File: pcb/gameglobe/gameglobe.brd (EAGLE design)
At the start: 49.5 x 99.1 mm, 12 parts

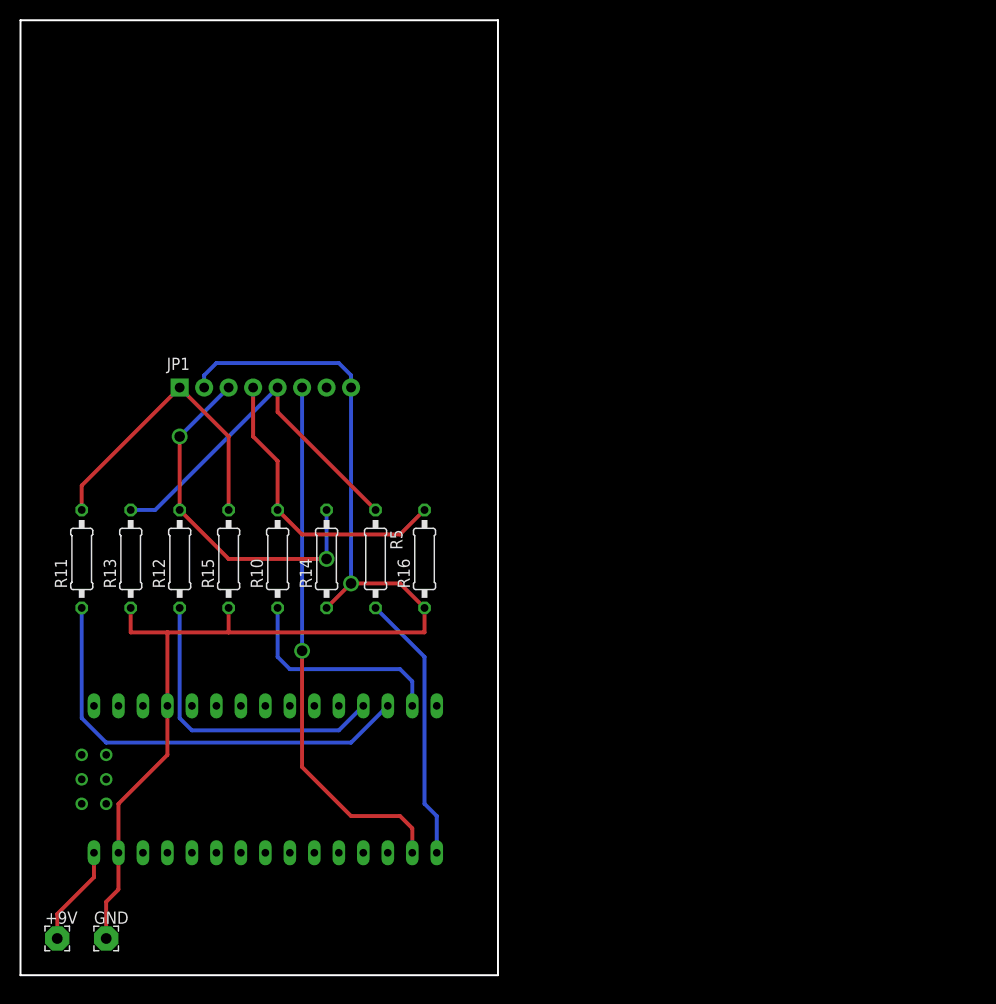
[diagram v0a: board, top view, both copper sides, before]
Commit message: BOM is sortof complete, and PCB is more complete-ish now
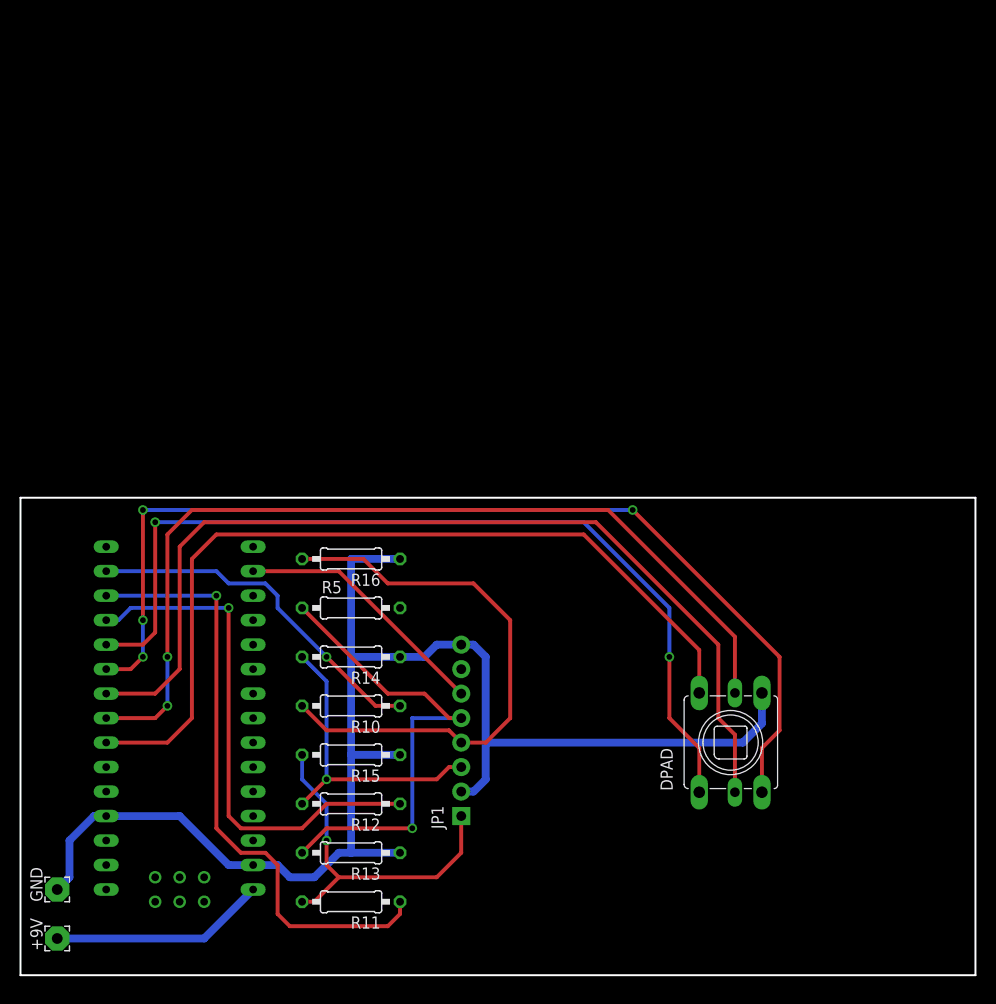
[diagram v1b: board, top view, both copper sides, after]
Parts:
- added DPAD: SKQUCAA010, gamaral:SKQU
- moved JP1 53.2 mm to (45.7, 16.5), turned to 90 degrees
- moved R11 45.2 mm to (34.3, 7.62), turned to 180 degrees
- moved R13 38.1 mm to (34.3, 12.7), turned to 180 degrees
- moved R12 31.0 mm to (34.3, 17.8), turned to 180 degrees
- moved R15 24.0 mm to (34.3, 22.9), turned to 180 degrees
- moved R10 17.0 mm to (34.3, 27.9), turned to 180 degrees
- moved R14 10.5 mm to (34.3, 33.0), turned to 180 degrees
- moved R16 7.62 mm to (34.3, 43.2), turned to 180 degrees
- moved GND 7.18 mm to (3.81, 8.89), turned to 90 degrees
- moved U$1 5.68 mm to (14.0, 17.8), turned to 0 degrees
- moved R5 5.68 mm to (34.3, 38.1), turned to 0 degrees
- turned +9V to 90 degrees
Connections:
- new net N$10: DPAD.CENTER, U$1.D4
- new net N$5: DPAD.UP, U$1.D8
- new net N$6: DPAD.DOWN, U$1.D7
- new net N$8: DPAD.LEFT, U$1.D6
- new net N$9: DPAD.RIGHT, U$1.D5
- net GND: now also DPAD.COMMON
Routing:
- net N$6: track 0.00 -> 106.7 mm, vias 0 -> 4
- net N$8: track 0.00 -> 99.6 mm
- net N$9: track 0.00 -> 95.9 mm, vias 0 -> 2
- net N$5: track 0.00 -> 94.5 mm, vias 0 -> 2
- net N$10: track 0.00 -> 89.6 mm
- net VCC_LCD: track 56.0 -> 26.9 mm, vias 1 -> 0
- net N$1: track 28.0 -> 0.00 mm
- net DIN_LCD: track 31.1 -> 58.6 mm
- net GND: track 123.9 -> 148.7 mm, vias 1 -> 0
- net N$4: track 32.1 -> 54.2 mm, vias 0 -> 1
- net N$3: track 45.8 -> 63.6 mm, vias 0 -> 1
- net N$2: track 22.6 -> 37.0 mm, vias 0 -> 1
- net CLK_LCD: track 37.4 -> 50.2 mm, vias 0 -> 1
- net N$7: track 10.5 -> 22.4 mm
- net DC_LCD: track 37.2 -> 31.8 mm, vias 2 -> 1
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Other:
- board size 49.5 x 99.1 mm -> 99.1 x 49.5 mm

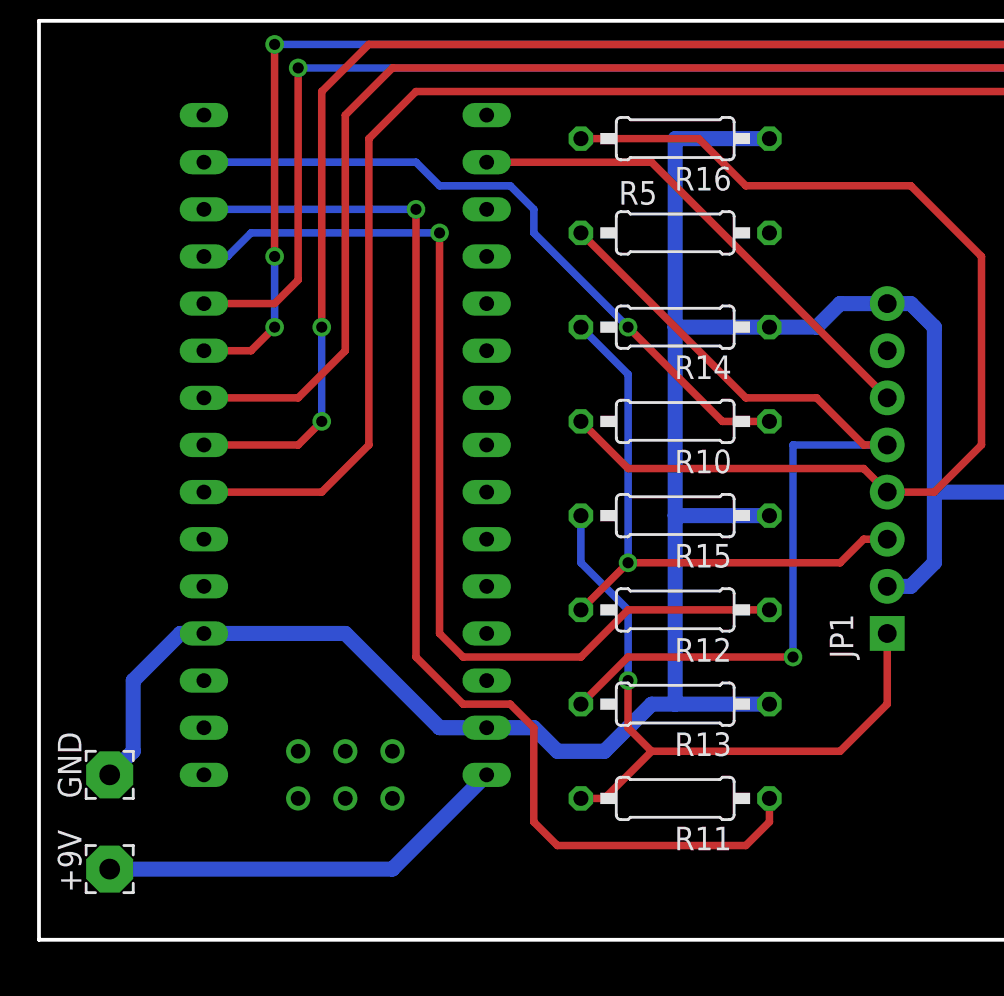
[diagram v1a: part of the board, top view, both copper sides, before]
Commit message: Add backlight wire and resistor
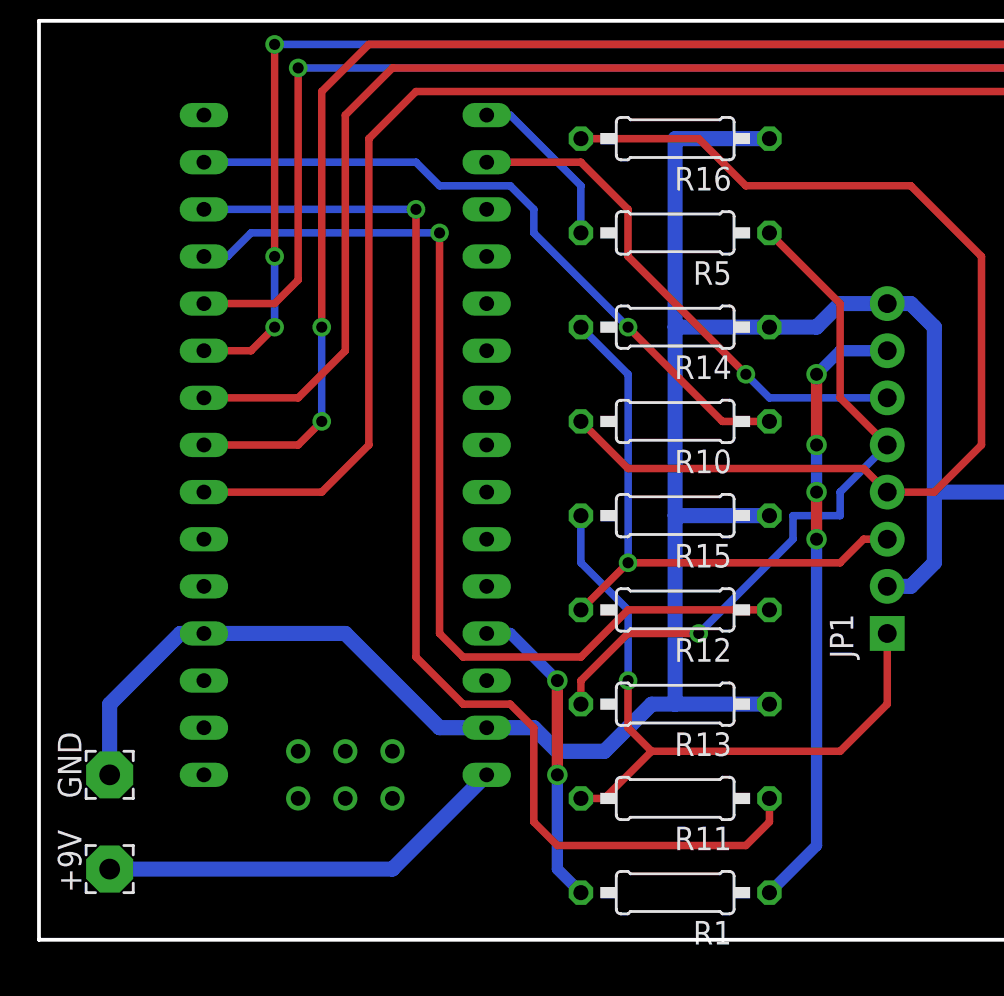
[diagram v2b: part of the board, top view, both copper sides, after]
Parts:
- added R1: 220, resistor:0207/10
- turned R5 to 180 degrees
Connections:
- removed net BL_LCD: JP1.7
- new net LED_LCD: JP1.7, R1.1
- new net N$11: R1.2, U$1.5V
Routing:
- net LED_LCD: track 0.00 -> 33.3 mm, vias 0 -> 4
- net N$11: track 0.00 -> 16.8 mm, vias 0 -> 2
- net CLK_LCD: track 50.2 -> 38.6 mm
- net N$1: track 0.00 -> 9.20 mm
- net VCC_LCD: track 26.9 -> 28.3 mm, vias 0 -> 1
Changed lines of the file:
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@@
 <element name="+9V" library="wirepad" package="2,54/1,1" value="WIREPAD2,54/1,1" x="3.81" y="3.81" rot="R90"/>
 <element name="GND" library="wirepad" package="2,54/1,1" value="WIREPAD2,54/1,1" x="3.81" y="8.89" rot="R90"/>
-<element name="R5" library="resistor" package="0207/10" value="10k" x="34.29" y="38.1"/>
+<element name="R5" library="resistor" package="0207/10" value="10k" x="34.29" y="38.1" rot="R180"/>
 <element name="R10" library="resistor" package="0207/10" value="10k" x="34.29" y="27.94" rot="R180"/>
 <element name="R11" library="resistor" package="0207/10" value="10k" x="34.29" y="7.62" rot="R180"/>
@@
 <attribute name="OC_ADAFRUIT" value="504" x="73.66" y="24.13" size="1.778" layer="27" rot="R90" display="off"/>
 </element>
+<element name="R1" library="resistor" package="0207/10" value="220" x="34.29" y="2.54" rot="R180"/>
 </elements>
 <signals>
@@
 <contactref element="GND" pad="1"/>
 <contactref element="DPAD" pad="COMMON"/>
-<wire x1="3.81" y1="8.89" x2="5.08" y2="10.16" width="0.8128" layer="16"/>
-<wire x1="5.08" y1="10.16" x2="5.08" y2="13.97" width="0.8128" layer="16"/>
-<wire x1="5.08" y1="13.97" x2="7.62" y2="16.51" width="0.8128" layer="16"/>
+<wire x1="3.81" y1="12.7" x2="7.62" y2="16.51" width="0.8128" layer="16"/>
 <wire x1="7.62" y1="16.51" x2="8.89" y2="16.51" width="0.8128" layer="16"/>
-<wire x1="8.89" y1="16.51" x2="16.51" y2="16.51" width="0.8128" layer="16"/>
+<wire x1="16.51" y1="16.51" x2="8.89" y2="16.51" width="0.8128" layer="16"/>
 <wire x1="16.51" y1="16.51" x2="21.59" y2="11.43" width="0.8128" layer="16"/>
 <wire x1="21.59" y1="11.43" x2="24.13" y2="11.43" width="0.8128" layer="16"/>
@@
 <wire x1="76.91" y1="26.11" x2="74.93" y2="24.13" width="0.8128" layer="16"/>
 <wire x1="74.93" y1="24.13" x2="48.26" y2="24.13" width="0.8128" layer="16"/>
+<wire x1="3.81" y1="12.7" x2="3.81" y2="8.89" width="0.8128" layer="16"/>
 </signal>
 <signal name="RST_LCD">
@@
 <contactref element="R13" pad="2"/>
 <contactref element="R5" pad="1"/>
-<wire x1="29.21" y1="12.7" x2="31.75" y2="15.24" width="0.4064" layer="1"/>
-<wire x1="31.75" y1="15.24" x2="40.64" y2="15.24" width="0.4064" layer="1"/>
-<via x="40.64" y="15.24" extent="1-16" drill="0.6" diameter="0.6096"/>
-<wire x1="40.64" y1="15.24" x2="40.64" y2="26.67" width="0.4064" layer="16"/>
-<wire x1="40.64" y1="26.67" x2="45.72" y2="26.67" width="0.4064" layer="16"/>
-<wire x1="45.72" y1="26.67" x2="44.45" y2="26.67" width="0.4064" layer="1"/>
-<wire x1="44.45" y1="26.67" x2="41.91" y2="29.21" width="0.4064" layer="1"/>
-<wire x1="41.91" y1="29.21" x2="38.1" y2="29.21" width="0.4064" layer="1"/>
-<wire x1="38.1" y1="29.21" x2="29.21" y2="38.1" width="0.4064" layer="1"/>
+<wire x1="29.21" y1="12.7" x2="29.21" y2="13.97" width="0.4064" layer="1"/>
+<wire x1="29.21" y1="13.97" x2="31.75" y2="16.51" width="0.4064" layer="1"/>
+<wire x1="31.75" y1="16.51" x2="35.56" y2="16.51" width="0.4064" layer="1"/>
+<via x="35.56" y="16.51" extent="1-16" drill="0.6" diameter="0.6096"/>
+<wire x1="45.72" y1="26.67" x2="43.18" y2="29.21" width="0.4064" layer="1"/>
+<wire x1="43.18" y1="29.21" x2="43.18" y2="34.29" width="0.4064" layer="1"/>
+<wire x1="43.18" y1="34.29" x2="39.37" y2="38.1" width="0.4064" layer="1"/>
+<wire x1="35.56" y1="16.51" x2="40.64" y2="21.59" width="0.4064" layer="16"/>
+<wire x1="40.64" y1="21.59" x2="40.64" y2="22.86" width="0.4064" layer="16"/>
+<wire x1="40.64" y1="22.86" x2="43.18" y2="22.86" width="0.4064" layer="16"/>
+<wire x1="43.18" y1="22.86" x2="43.18" y2="24.13" width="0.4064" layer="16"/>
+<wire x1="43.18" y1="24.13" x2="45.72" y2="26.67" width="0.4064" layer="16"/>
 </signal>
 <signal name="VCC_LCD">
 <contactref element="JP1" pad="6"/>
 <contactref element="U$1" pad="3.3V"/>
-<wire x1="24.13" y1="41.91" x2="33.02" y2="41.91" width="0.4064" layer="1"/>
-<wire x1="33.02" y1="41.91" x2="45.72" y2="29.21" width="0.4064" layer="1"/>
-</signal>
-<signal name="BL_LCD">
+<wire x1="45.72" y1="29.21" x2="39.37" y2="29.21" width="0.4064" layer="16"/>
+<wire x1="39.37" y1="29.21" x2="38.1" y2="30.48" width="0.4064" layer="16"/>
+<via x="38.1" y="30.48" extent="1-16" drill="0.6" diameter="0.6096"/>
+<wire x1="38.1" y1="30.48" x2="31.75" y2="36.83" width="0.4064" layer="1"/>
+<wire x1="31.75" y1="36.83" x2="31.75" y2="39.37" width="0.4064" layer="1"/>
+<wire x1="31.75" y1="39.37" x2="29.21" y2="41.91" width="0.4064" layer="1"/>
+<wire x1="29.21" y1="41.91" x2="24.13" y2="41.91" width="0.4064" layer="1"/>
+</signal>
+<signal name="LED_LCD">
 <contactref element="JP1" pad="7"/>
+<contactref element="R1" pad="1"/>
+<wire x1="39.37" y1="2.54" x2="41.91" y2="5.08" width="0.6096" layer="16"/>
+<wire x1="41.91" y1="5.08" x2="41.91" y2="21.59" width="0.6096" layer="16"/>
+<via x="41.91" y="21.59" extent="1-16" drill="0.7" diameter="0.8128"/>
+<wire x1="41.91" y1="21.59" x2="41.91" y2="24.13" width="0.6096" layer="1"/>
+<via x="41.91" y="24.13" extent="1-16" drill="0.7" diameter="0.8128"/>
+<wire x1="41.91" y1="24.13" x2="41.91" y2="26.67" width="0.6096" layer="16"/>
+<via x="41.91" y="26.67" extent="1-16" drill="0.7" diameter="0.8128"/>
+<wire x1="41.91" y1="26.67" x2="41.91" y2="30.48" width="0.6096" layer="1"/>
+<via x="41.91" y="30.48" extent="1-16" drill="0.7" diameter="0.8128"/>
+<wire x1="41.91" y1="30.48" x2="43.18" y2="31.75" width="0.6096" layer="16"/>
+<wire x1="43.18" y1="31.75" x2="45.72" y2="31.75" width="0.6096" layer="16"/>
 </signal>
 <signal name="N$1">
 <contactref element="U$1" pad="D13"/>
 <contactref element="R5" pad="2"/>
-<wire x1="24.13" y1="44.45" x2="39.37" y2="38.1" width="0" layer="19" extent="1-1"/>
+<wire x1="24.13" y1="44.45" x2="25.4" y2="44.45" width="0.4064" layer="16"/>
+<wire x1="25.4" y1="44.45" x2="29.21" y2="40.64" width="0.4064" layer="16"/>
+<wire x1="29.21" y1="40.64" x2="29.21" y2="38.1" width="0.4064" layer="16"/>
 </signal>
 <signal name="N$2">
@@
 <wire x1="15.24" y1="24.13" x2="8.89" y2="24.13" width="0.4064" layer="1"/>
 </signal>
+<signal name="N$11">
+<contactref element="U$1" pad="5V"/>
+<contactref element="R1" pad="2"/>
+<wire x1="24.13" y1="16.51" x2="25.4" y2="16.51" width="0.6096" layer="16"/>
+<wire x1="25.4" y1="16.51" x2="27.94" y2="13.97" width="0.6096" layer="16"/>
+<via x="27.94" y="13.97" extent="1-16" drill="0.7" diameter="0.8128"/>
+<wire x1="27.94" y1="13.97" x2="27.94" y2="8.89" width="0.6096" layer="1"/>
+<via x="27.94" y="8.89" extent="1-16" drill="0.7" diameter="0.8128"/>
+<wire x1="27.94" y1="8.89" x2="27.94" y2="3.81" width="0.6096" layer="16"/>
+<wire x1="27.94" y1="3.81" x2="29.21" y2="2.54" width="0.6096" layer="16"/>
+</signal>
 </signals>

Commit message: Improve net names and board layout
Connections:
- net CLK_LCD renamed LCD_CLK
- net DC_LCD renamed LCD_DC
- net DIN_LCD renamed LCD_DIN
- net LED_LCD renamed LCD_LED
- net N$10 renamed DPAD_CENTER
- net N$5 renamed DPAD_UP
- net N$6 renamed DPAD_DOWN
- net N$8 renamed DPAD_LEFT
- net N$9 renamed DPAD_RIGHT
- net RST_LCD renamed LCD_RST
- net VCC_LCD renamed LCD_VCC
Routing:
- net LCD_DIN: track 58.6 -> 34.4 mm, vias 0 -> 1
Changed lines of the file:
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@@
 </class>
 </classes>
-<designrules name="default">
+<designrules name="custom">
 <description language="de">&lt;b&gt;EAGLE Design Rules&lt;/b&gt;
 &lt;p&gt;
@@
 <param name="mdViaViaSameLayer" value="8mil"/>
 <param name="mnLayersViaInSmd" value="2"/>
-<param name="mdCopperDimension" value="40mil"/>
+<param name="mdCopperDimension" value="20mil"/>
 <param name="mdDrill" value="8mil"/>
 <param name="mdSmdStop" value="0mil"/>
 <param name="msWidth" value="10mil"/>
-<param name="msDrill" value="24mil"/>
+<param name="msDrill" value="20mil"/>
 <param name="msMicroVia" value="9.99mm"/>
 <param name="msBlindViaRatio" value="0.5"/>
@@
 <param name="dpGapFactor" value="2.5"/>
 <param name="checkGrid" value="0"/>
-<param name="checkAngle" value="0"/>
+<param name="checkAngle" value="1"/>
 <param name="checkFont" value="1"/>
 <param name="checkRestrict" value="1"/>
@@
 <wire x1="3.81" y1="12.7" x2="3.81" y2="8.89" width="0.8128" layer="16"/>
 </signal>
-<signal name="RST_LCD">
+<signal name="LCD_RST">
 <contactref element="JP1" pad="1"/>
 <contactref element="R11" pad="2"/>
@@
 <wire x1="31.75" y1="11.43" x2="33.02" y2="10.16" width="0.4064" layer="1"/>
 </signal>
-<signal name="DC_LCD">
+<signal name="LCD_DC">
 <contactref element="JP1" pad="3"/>
 <contactref element="R12" pad="2"/>
@@
 <wire x1="31.75" y1="20.32" x2="43.18" y2="20.32" width="0.4064" layer="1"/>
 </signal>
-<signal name="DIN_LCD">
+<signal name="LCD_DIN">
 <contactref element="JP1" pad="4"/>
 <contactref element="R10" pad="2"/>
 <contactref element="R16" pad="2"/>
-<wire x1="29.21" y1="43.18" x2="35.56" y2="43.18" width="0.4064" layer="1"/>
-<wire x1="35.56" y1="43.18" x2="38.1" y2="40.64" width="0.4064" layer="1"/>
-<wire x1="38.1" y1="40.64" x2="46.99" y2="40.64" width="0.4064" layer="1"/>
-<wire x1="46.99" y1="40.64" x2="50.8" y2="36.83" width="0.4064" layer="1"/>
-<wire x1="50.8" y1="36.83" x2="50.8" y2="26.67" width="0.4064" layer="1"/>
-<wire x1="50.8" y1="26.67" x2="48.26" y2="24.13" width="0.4064" layer="1"/>
-<wire x1="48.26" y1="24.13" x2="45.72" y2="24.13" width="0.4064" layer="1"/>
 <wire x1="29.21" y1="27.94" x2="31.75" y2="25.4" width="0.4064" layer="1"/>
 <wire x1="31.75" y1="25.4" x2="44.45" y2="25.4" width="0.4064" layer="1"/>
 <wire x1="44.45" y1="25.4" x2="45.72" y2="24.13" width="0.4064" layer="1"/>
-</signal>
-<signal name="CLK_LCD">
+<via x="30.48" y="36.83" extent="1-16" drill="0.6" diameter="0.8128"/>
+<wire x1="30.48" y1="36.83" x2="30.48" y2="41.91" width="0.4064" layer="16"/>
+<wire x1="30.48" y1="41.91" x2="29.21" y2="43.18" width="0.4064" layer="16"/>
+<wire x1="29.21" y1="27.94" x2="30.48" y2="29.21" width="0.4064" layer="1"/>
+<wire x1="30.48" y1="29.21" x2="30.48" y2="36.83" width="0.4064" layer="1"/>
+</signal>
+<signal name="LCD_CLK">
 <contactref element="JP1" pad="5"/>
 <contactref element="R13" pad="2"/>
@@
 <wire x1="43.18" y1="24.13" x2="45.72" y2="26.67" width="0.4064" layer="16"/>
 </signal>
-<signal name="VCC_LCD">
+<signal name="LCD_VCC">
 <contactref element="JP1" pad="6"/>
 <contactref element="U$1" pad="3.3V"/>
@@
 <wire x1="29.21" y1="41.91" x2="24.13" y2="41.91" width="0.4064" layer="1"/>
 </signal>
-<signal name="LED_LCD">
+<signal name="LCD_LED">
 <contactref element="JP1" pad="7"/>
 <contactref element="R1" pad="1"/>
@@
 <wire x1="31.75" y1="17.78" x2="39.37" y2="17.78" width="0.4064" layer="1"/>
 </signal>
-<signal name="N$5">
+<signal name="DPAD_UP">
 <contactref element="U$1" pad="D8"/>
 <contactref element="DPAD" pad="UP"/>
@@
 <wire x1="12.7" y1="34.29" x2="8.89" y2="34.29" width="0.4064" layer="1"/>
 </signal>
-<signal name="N$6">
+<signal name="DPAD_DOWN">
 <contactref element="DPAD" pad="DOWN"/>
 <contactref element="U$1" pad="D7"/>
@@
 <wire x1="63.5" y1="48.26" x2="78.74" y2="33.02" width="0.4064" layer="1"/>
 </signal>
-<signal name="N$8">
+<signal name="DPAD_LEFT">
 <contactref element="DPAD" pad="LEFT"/>
 <contactref element="U$1" pad="D6"/>
@@
 <wire x1="13.97" y1="29.21" x2="8.89" y2="29.21" width="0.4064" layer="1"/>
 </signal>
-<signal name="N$9">
+<signal name="DPAD_RIGHT">
 <contactref element="DPAD" pad="RIGHT"/>
 <contactref element="U$1" pad="D5"/>
@@
 <wire x1="74.11" y1="35.11" x2="60.96" y2="48.26" width="0.4064" layer="1"/>
 </signal>
-<signal name="N$10">
+<signal name="DPAD_CENTER">
 <contactref element="DPAD" pad="CENTER"/>
 <contactref element="U$1" pad="D4"/>
